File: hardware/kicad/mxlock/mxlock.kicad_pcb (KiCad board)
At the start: 2 copper layers, 60.4 x 49.1 mm, 21 parts, among them J1 ATMEL-ICE-10, J2 Conn_01x06, J3 Conn_01x02, J4 Conn_01x02, J5 Conn_01x02, Q1 2N3904, SW1 SW_SL, SW2 SW_CAPS, SW3 SW_4080, U1 CD4066BM, U2 ATtiny214/414/814

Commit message: Use "mxlock" for project files
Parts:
- J1: footprint stevekey:PinHeader_2x05_P1.27mm_Shrouded_Vertical_SMD_Handsolder -> mxlock:PinHeader_2x05_P1.27mm_Shrouded_Vertical_SMD_Handsolder
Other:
- board text added: "mxlock MCU DEV BOARD REV. 2 © 2023 MIKE NABEREZNY"
- board text removed: "STEVEKEY MCU DEV BOARD REV. 2 © 2023 MIKE NABEREZNY"
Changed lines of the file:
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@@
     (descr "Resistor, Axial_DIN0204 series, Axial, Horizontal, pin pitch=7.62mm, 0.167W, length*diameter=3.6*1.6mm^2, http://cdn-reichelt.de/documents/datenblatt/B400/1_4W%23YAG.pdf")
     (tags "Resistor Axial_DIN0204 series Axial Horizontal pin pitch 7.62mm 0.167W length 3.6mm diameter 1.6mm")
-    (property "Sheetfile" "stevekey.kicad_sch")
+    (property "Sheetfile" "mxlock.kicad_sch")
     (property "Sheetname" "")
     (property "ki_description" "Resistor, small US symbol")
@@
     (descr "Cherry MX keyswitch, 1.00u, PCB mount, http://cherryamericas.com/wp-content/uploads/2014/12/mx_cat.pdf")
     (tags "Cherry MX keyswitch 1.00u PCB")
-    (property "Sheetfile" "stevekey.kicad_sch")
+    (property "Sheetfile" "mxlock.kicad_sch")
     (property "Sheetname" "")
     (property "ki_description" "Push button switch, generic, two pins")
@@
     (descr "LED, diameter 5.0mm, 2 pins, http://cdn-reichelt.de/documents/datenblatt/A500/LL-504BC2E-009.pdf")
     (tags "LED diameter 5.0mm 2 pins")
-    (property "Sheetfile" "stevekey.kicad_sch")
+    (property "Sheetfile" "mxlock.kicad_sch")
     (property "Sheetname" "")
     (property "ki_description" "Light emitting diode")
@@
     (descr "C, Disc series, Radial, pin pitch=5.00mm, , diameter*width=5*2.5mm^2, Capacitor, http://cdn-reichelt.de/documents/datenblatt/B300/DS_KERKO_TC.pdf")
     (tags "C Disc series Radial pin pitch 5.00mm  diameter 5mm width 2.5mm Capacitor")
-    (property "Sheetfile" "stevekey.kicad_sch")
+    (property "Sheetfile" "mxlock.kicad_sch")
     (property "Sheetname" "")
     (property "ki_description" "Unpolarized capacitor, small symbol")
@@
     (descr "TO-92 leads in-line, narrow, oval pads, drill 0.75mm (see NXP sot054_po.pdf)")
     (tags "to-92 sc-43 sc-43a sot54 PA33 transistor")
-    (property "Sheetfile" "stevekey.kicad_sch")
+    (property "Sheetfile" "mxlock.kicad_sch")
     (property "Sheetname" "")
     (property "ki_description" "0.2A Ic, 40V Vce, Small Signal NPN Transistor, TO-92")
@@
     (descr "Through hole straight pin header, 1x02, 2.54mm pitch, single row")
     (tags "Through hole pin header THT 1x02 2.54mm single row")
-    (property "Sheetfile" "stevekey.kicad_sch")
+    (property "Sheetfile" "mxlock.kicad_sch")
     (property "Sheetname" "")
     (property "ki_description" "Generic connector, single row, 01x02, script generated (kicad-library-utils/schlib/autogen/connector/)")
@@
     (descr "SOIC, 14 Pin (JEDEC MS-012AB, https://www.analog.com/media/en/package-pcb-resources/package/pkg_pdf/soic_narrow-r/r_14.pdf), generated with kicad-footprint-generator ipc_gullwing_generator.py")
     (tags "SOIC SO")
-    (property "Sheetfile" "stevekey.kicad_sch")
+    (property "Sheetfile" "mxlock.kicad_sch")
     (property "Sheetname" "")
     (property "ki_description" "20MHz, 2kB Flash, 128B SRAM, 64B EEPROM, SOIC-14")
@@
     (descr "C, Disc series, Radial, pin pitch=5.00mm, , diameter*width=5*2.5mm^2, Capacitor, http://cdn-reichelt.de/documents/datenblatt/B300/DS_KERKO_TC.pdf")
     (tags "C Disc series Radial pin pitch 5.00mm  diameter 5mm width 2.5mm Capacitor")
-    (property "Sheetfile" "stevekey.kicad_sch")
+    (property "Sheetfile" "mxlock.kicad_sch")
     (property "Sheetname" "")
     (property "ki_description" "Unpolarized capacitor, small symbol")
@@
     (descr "Cherry MX keyswitch, 1.00u, PCB mount, http://cherryamericas.com/wp-content/uploads/2014/12/mx_cat.pdf")
     (tags "Cherry MX keyswitch 1.00u PCB")
-    (property "Sheetfile" "stevekey.kicad_sch")
+    (property "Sheetfile" "mxlock.kicad_sch")
     (property "Sheetname" "")
     (property "ki_description" "Push button switch, generic, two pins")
@@
     (descr "LED, diameter 5.0mm, 2 pins, http://cdn-reichelt.de/documents/datenblatt/A500/LL-504BC2E-009.pdf")
     (tags "LED diameter 5.0mm 2 pins")
-    (property "Sheetfile" "stevekey.kicad_sch")
+    (property "Sheetfile" "mxlock.kicad_sch")
     (property "Sheetname" "")
     (property "ki_description" "Light emitting diode")
@@
     (descr "Resistor, Axial_DIN0204 series, Axial, Horizontal, pin pitch=7.62mm, 0.167W, length*diameter=3.6*1.6mm^2, http://cdn-reichelt.de/documents/datenblatt/B400/1_4W%23YAG.pdf")
     (tags "Resistor Axial_DIN0204 series Axial Horizontal pin pitch 7.62mm 0.167W length 3.6mm diameter 1.6mm")
-    (property "Sheetfile" "stevekey.kicad_sch")
+    (property "Sheetfile" "mxlock.kicad_sch")
     (property "Sheetname" "")
     (property "ki_description" "Resistor, small US symbol")
@@
     (descr "Cherry MX keyswitch, 1.00u, PCB mount, http://cherryamericas.com/wp-content/uploads/2014/12/mx_cat.pdf")
     (tags "Cherry MX keyswitch 1.00u PCB")
-    (property "Sheetfile" "stevekey.kicad_sch")
+    (property "Sheetfile" "mxlock.kicad_sch")
     (property "Sheetname" "")
     (property "ki_description" "Push button switch, generic, two pins")
@@
     (descr "Through hole straight pin header, 1x06, 2.54mm pitch, single row")
     (tags "Through hole pin header THT 1x06 2.54mm single row")
-    (property "Sheetfile" "stevekey.kicad_sch")
+    (property "Sheetfile" "mxlock.kicad_sch")
     (property "Sheetname" "")
     (property "ki_description" "Generic connector, single row, 01x06, script generated (kicad-library-utils/schlib/autogen/connector/)")
@@
     (descr "SO, 14 Pin (https://www.st.com/resource/en/datasheet/l6491.pdf), generated with kicad-footprint-generator ipc_gullwing_generator.py")
     (tags "SO SO")
-    (property "Sheetfile" "stevekey.kicad_sch")
+    (property "Sheetfile" "mxlock.kicad_sch")
     (property "Sheetname" "")
     (property "ki_description" "Quad 20V analog SPST 1:1 switch, SO-14 (3.9x8.65mm)")
@@
     (descr "Resistor, Axial_DIN0204 series, Axial, Horizontal, pin pitch=7.62mm, 0.167W, length*diameter=3.6*1.6mm^2, http://cdn-reichelt.de/documents/datenblatt/B400/1_4W%23YAG.pdf")
     (tags "Resistor Axial_DIN0204 series Axial Horizontal pin pitch 7.62mm 0.167W length 3.6mm diameter 1.6mm")
-    (property "Sheetfile" "stevekey.kicad_sch")
+    (property "Sheetfile" "mxlock.kicad_sch")
     (property "Sheetname" "")
     (property "ki_description" "Resistor, small US symbol")
@@
     (descr "Through hole straight pin header, 1x02, 2.54mm pitch, single row")
     (tags "Through hole pin header THT 1x02 2.54mm single row")
-    (property "Sheetfile" "stevekey.kicad_sch")
+    (property "Sheetfile" "mxlock.kicad_sch")
     (property "Sheetname" "")
     (property "ki_description" "Generic connector, single row, 01x02, script generated (kicad-library-utils/schlib/autogen/connector/)")
@@
     (descr "CP, Radial series, Radial, pin pitch=2.50mm, , diameter=6.3mm, Electrolytic Capacitor")
     (tags "CP Radial series Radial pin pitch 2.50mm  diameter 6.3mm Electrolytic Capacitor")
-    (property "Sheetfile" "stevekey.kicad_sch")
+    (property "Sheetfile" "mxlock.kicad_sch")
     (property "Sheetname" "")
     (property "ki_description" "Polarized capacitor, small symbol")
@@
     )
   )
-  (footprint "stevekey:PinHeader_2x05_P1.27mm_Shrouded_Vertical_SMD_Handsolder" (layer "F.Cu")
+  (footprint "mxlock:PinHeader_2x05_P1.27mm_Shrouded_Vertical_SMD_Handsolder" (layer "F.Cu")
     (at 114.723 77.056 180)
-    (property "Sheetfile" "stevekey.kicad_sch")
+    (property "Sheetfile" "mxlock.kicad_sch")
     (property "Sheetname" "")
     (property "ki_description" "Atmel 10-pin JTAG connector")
@@
     (descr "LED, diameter 5.0mm, 2 pins, http://cdn-reichelt.de/documents/datenblatt/A500/LL-504BC2E-009.pdf")
     (tags "LED diameter 5.0mm 2 pins")
-    (property "Sheetfile" "stevekey.kicad_sch")
+    (property "Sheetfile" "mxlock.kicad_sch")
     (property "Sheetname" "")
     (property "ki_description" "Light emitting diode")
@@
     (descr "Through hole straight pin header, 1x02, 2.54mm pitch, single row")
     (tags "Through hole pin header THT 1x02 2.54mm single row")
-    (property "Sheetfile" "stevekey.kicad_sch")
+    (property "Sheetfile" "mxlock.kicad_sch")
     (property "Sheetname" "")
     (property "ki_description" "Generic connector, single row, 01x02, script generated (kicad-library-utils/schlib/autogen/connector/)")
@@
     (descr "Resistor, Axial_DIN0204 series, Axial, Horizontal, pin pitch=7.62mm, 0.167W, length*diameter=3.6*1.6mm^2, http://cdn-reichelt.de/documents/datenblatt/B400/1_4W%23YAG.pdf")
     (tags "Resistor Axial_DIN0204 series Axial Horizontal pin pitch 7.62mm 0.167W length 3.6mm diameter 1.6mm")
-    (property "Sheetfile" "stevekey.kicad_sch")
+    (property "Sheetfile" "mxlock.kicad_sch")
     (property "Sheetname" "")
     (property "ki_description" "Resistor, small US symbol")
@@
   (gr_rect (start 108.2802 71.1232) (end 168.7036 120.1832)
     (stroke (width 0.1) (type default)) (fill none) (layer "Edge.Cuts"))
-  (gr_text "STEVEKEY MCU DEV BOARD REV. 2 © 2023 MIKE NABEREZNY" (at 161.4 118.8) (layer "B.SilkS")
+  (gr_text "mxlock MCU DEV BOARD REV. 2 © 2023 MIKE NABEREZNY" (at 161.4 118.8) (layer "B.SilkS")
     (effects (font (size 1 1) (thickness 0.15)) (justify left bottom mirror))
   )

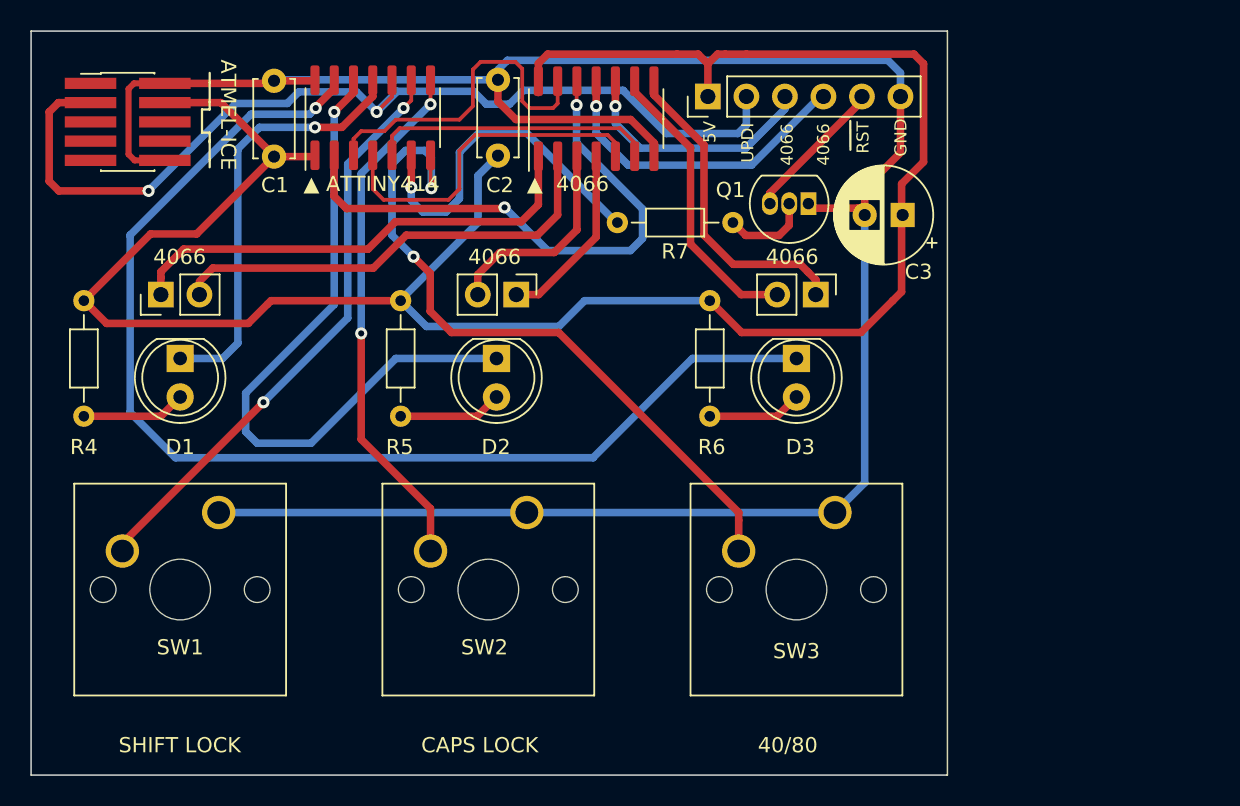
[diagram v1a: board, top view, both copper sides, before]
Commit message: Add fourth key to the PCB layout
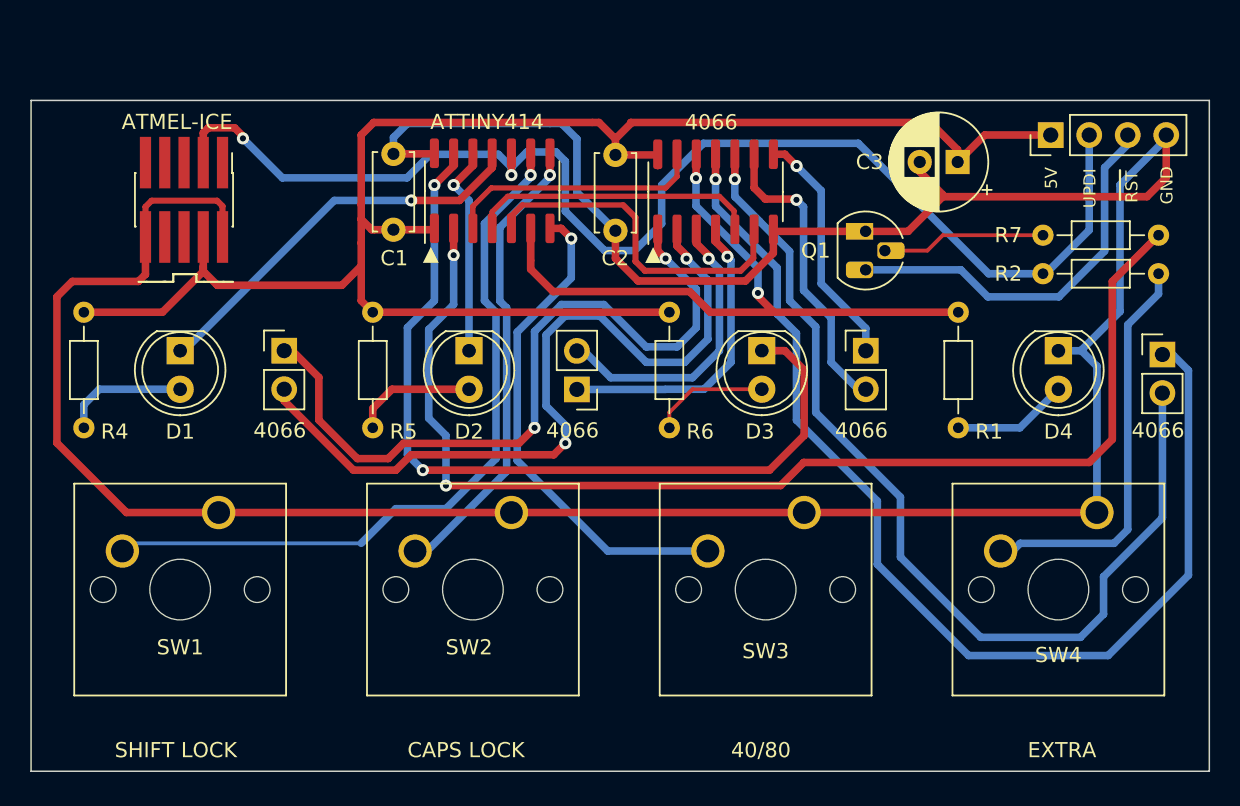
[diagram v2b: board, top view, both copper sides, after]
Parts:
- added D4: LED, LED_THT:LED_D5.0mm, F.Cu at (176.0, 92.2)
- added J6: Conn_01x02, Connector_PinHeader_2.54mm:PinHeader_1x02_P2.54mm_Vertical, F.Cu at (182.9, 92.5)
- added R1: 330, Resistor_THT:R_Axial_DIN0204_L3.6mm_D1.6mm_P7.62mm_Horizontal, F.Cu at (169.4, 89.7)
- added R2: 1K, Resistor_THT:R_Axial_DIN0204_L3.6mm_D1.6mm_P7.62mm_Horizontal, F.Cu at (182.6, 87.1)
- added SW4: SW_EXTRA, Button_Switch_Keyboard:SW_Cherry_MX_1.00u_PCB, F.Cu at (178.6, 102.9)
- J2: value Conn_01x06 -> Conn_01x04; footprint Connector_PinHeader_2.54mm:PinHeader_1x06_P2.54mm_Vertical -> Connector_PinHeader_2.54mm:PinHeader_1x04_P2.54mm_Vertical
- Q1: footprint Package_TO_SOT_THT:TO-92_Inline -> Package_TO_SOT_THT:TO-92_HandSolder
- moved R7 35.7 mm to (182.6, 84.6), turned to 180 degrees
- moved J2 22.7 mm to (175.5, 78.0)
- moved C1 9.23 mm to (132.2, 84.2)
- moved U2 9.23 mm to (138.7, 81.7)
- moved U1 9.23 mm to (153.4, 81.7)
- moved J3 8.93 mm to (125.0, 92.2), turned to 0 degrees
- moved C2 7.75 mm to (146.8, 79.3), turned to -90 degrees
- moved J4 7.42 mm to (144.3, 94.8), turned to 180 degrees
- moved J1 6.43 mm to (118.4, 82.3), turned to 90 degrees
- moved C3 5.04 mm to (169.4, 79.8)
- moved J5 4.96 mm to (163.3, 92.2), turned to 0 degrees
- moved Q1 4.19 mm to (163.3, 84.3), turned to -90 degrees
- moved R6 2.77 mm to (150.4, 89.7)
- moved D3 2.34 mm to (156.5, 92.2)
- moved SW3 2.03 mm to (159.3, 102.9)
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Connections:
- J2 pad 3: EXTRA1 -> Net-(J2-Pin_3)
- J2 pad 4: EXTRA0 -> GND
- Q1 pad 3: Net-(J2-Pin_5) -> Net-(J2-Pin_3)
- R7 pad 1: CBMRESETOUT -> /CBMRESETOUT
- U1 pad 10: EXTRA1 -> Net-(J6-Pin_2)
- U1 pad 11: EXTRA0 -> Net-(J6-Pin_1)
- U2 pad 2: EXOUT -> /CBMRESETOUT
- U2 pad 6: CBMRESETOUT -> EXOUT
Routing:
- net /CBMRESETOUT: track 0.00 -> 78.1 mm, vias 0 -> 2
- net Net-(J6-Pin_1): track 0.00 -> 72.3 mm, vias 0 -> 1
- net Net-(J6-Pin_2): track 0.00 -> 64.0 mm, vias 0 -> 1
- net GND: track 152.6 -> 201.6 mm
- net /NCAPSLED: track 45.3 -> 14.0 mm
- net VCC: track 145.2 -> 114.1 mm
- net Net-(R2-Pad1): track 0.00 -> 26.7 mm
- net Net-(J2-Pin_3): track 0.00 -> 26.4 mm
- net CBMRESETOUT: track 23.9 -> 0.00 mm, vias 1 -> 0
- net Net-(J3-Pin_2): track 29.3 -> 50.8 mm, vias 0 -> 2
- net UPDI: track 64.4 -> 85.8 mm
- net /N4080LED: track 77.8 -> 56.5 mm, vias 1 -> 2
- net EXTRA0: track 21.2 -> 0.00 mm, vias 1 -> 0
- net Net-(J3-Pin_1): track 30.6 -> 48.9 mm, vias 0 -> 2
- net EXTRA1: track 16.5 -> 0.00 mm, vias 1 -> 0
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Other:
- board size 60.4 x 49.1 mm -> 77.7 x 44.2 mm
- board text added: "ATTINY414"
- board text added: "EXTRA"
- board text added: "MXLOCK DEMO BOARD REV. 2 © 2023 MIKE NABEREZNY"
- board text added: "▲"
- board text removed: "mxlock MCU DEV BOARD REV. 2 © 2023 MIKE NABEREZNY"
- board text removed: "▲ 4066"
- board text removed: "▲ ATTINY414"

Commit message: Use consistent reference designators
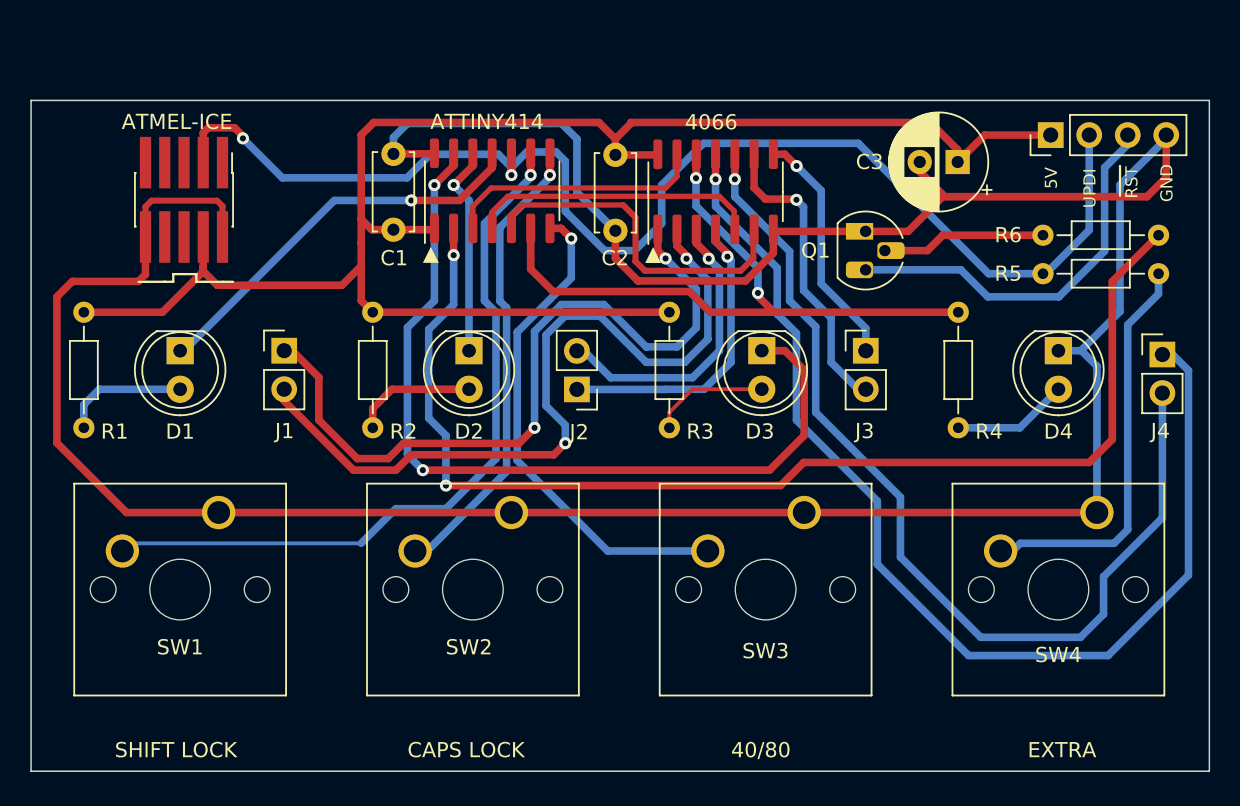
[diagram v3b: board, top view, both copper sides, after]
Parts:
- renumbered J3 to J1, J4 to J2, J5 to J3, J6 to J4, J2 to J5, J1 to J6, R4 to R1, R5 to R2, R6 to R3, R1 to R4, R2 to R5, R7 to R6, U2 to U1, U1 to U2

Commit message: Rename keys to LOCK0-3
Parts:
- SW1: value SW_SL -> SW_MX
- SW2: value SW_CAPS -> SW_MX
- SW3: value SW_4080 -> SW_MX
- SW4: value SW_EXTRA -> SW_MX
- moved J4 2.31 mm to (182.7, 94.8), turned to 180 degrees
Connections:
- net /CBMRESETOUT renamed /RESET_OUT
- net /N4080LED renamed /NLOCK2_LED
- net /NCAPSLED renamed /NLOCK1_LED
- net /NSLLED renamed /NLOCK0_LED
- net 4080OUT renamed LOCK2_OUT
- net CAPSOUT renamed LOCK1_OUT
- net EXOUT renamed LOCK3_OUT
- net N4080KEY renamed NLOCK2_KEY
- net NCAPSKEY renamed NLOCK1_KEY
- net NSLKEY renamed NLOCK0_KEY
- net SLOUT renamed LOCK0_OUT
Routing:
- net Net-(J4-Pin_2): track 64.0 -> 67.9 mm
- net Net-(J4-Pin_1): track 72.3 -> 68.7 mm
- net Net-(R5-Pad1): track 26.7 -> 27.6 mm
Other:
- board text added: "LOCK0"
- board text added: "LOCK1"
- board text added: "LOCK2"
- board text added: "LOCK3"
- board text removed: "40/80"
- board text removed: "CAPS LOCK"
- board text removed: "EXTRA"
- board text removed: "SHIFT LOCK"

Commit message: Minor layout tweaks
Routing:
- net /RESET_OUT: track 78.1 -> 79.0 mm
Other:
- board size 77.7 x 44.2 mm -> 77.6 x 44.2 mm

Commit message: Outline reset circuit on schematic
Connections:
- net Net-(J5-Pin_3) renamed /NRESET
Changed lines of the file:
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@@
   (net 27 "Net-(J2-Pin_1)")
   (net 28 "Net-(J2-Pin_2)")
-  (net 29 "Net-(J5-Pin_3)")
+  (net 29 "/NRESET")
   (net 30 "unconnected-(J6-TCK-Pad1)")
   (net 31 "unconnected-(J6-TMS-Pad5)")
@@
       (net 21 "Net-(Q1-B)") (pinfunction "B") (pintype "passive"))
     (pad "3" thru_hole roundrect (at 2.54 0 270) (size 1.1 1.8) (drill 0.75 (offset 0 0.4)) (layers "*.Cu" "*.Mask") (roundrect_rratio 0.25)
-      (net 29 "Net-(J5-Pin_3)") (pinfunction "C") (pintype "passive"))
+      (net 29 "/NRESET") (pinfunction "C") (pintype "passive"))
     (model "${KICAD6_3DMODEL_DIR}/Package_TO_SOT_THT.3dshapes/TO-92.wrl"
       (offset (xyz 0 0 0))
@@
       (net 13 "UPDI") (pinfunction "Pin_2") (pintype "passive"))
     (pad "3" thru_hole oval (at 0 5.08 90) (size 1.7 1.7) (drill 1) (layers "*.Cu" "*.Mask")
-      (net 29 "Net-(J5-Pin_3)") (pinfunction "Pin_3") (pintype "passive"))
+      (net 29 "/NRESET") (pinfunction "Pin_3") (pintype "passive"))
     (pad "4" thru_hole oval (at 0 7.62 90) (size 1.7 1.7) (drill 1) (layers "*.Cu" "*.Mask")
       (net 4 "GND") (pinfunction "Pin_4") (pintype "passive"))
